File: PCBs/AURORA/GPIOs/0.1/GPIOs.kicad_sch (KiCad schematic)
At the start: 25 parts, among them J1 Conn_01x02_Pin, J10 Conn_01x02_Pin, J11 Conn_01x02_Pin, J12 Conn_01x02_Pin, J13 Conn_01x02_Pin, J14 Conn_01x02_Pin, J15 Conn_01x02_Pin, J16 Conn_01x02_Pin, J17 Conn_01x05_Pin, J2 Conn_01x02_Pin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

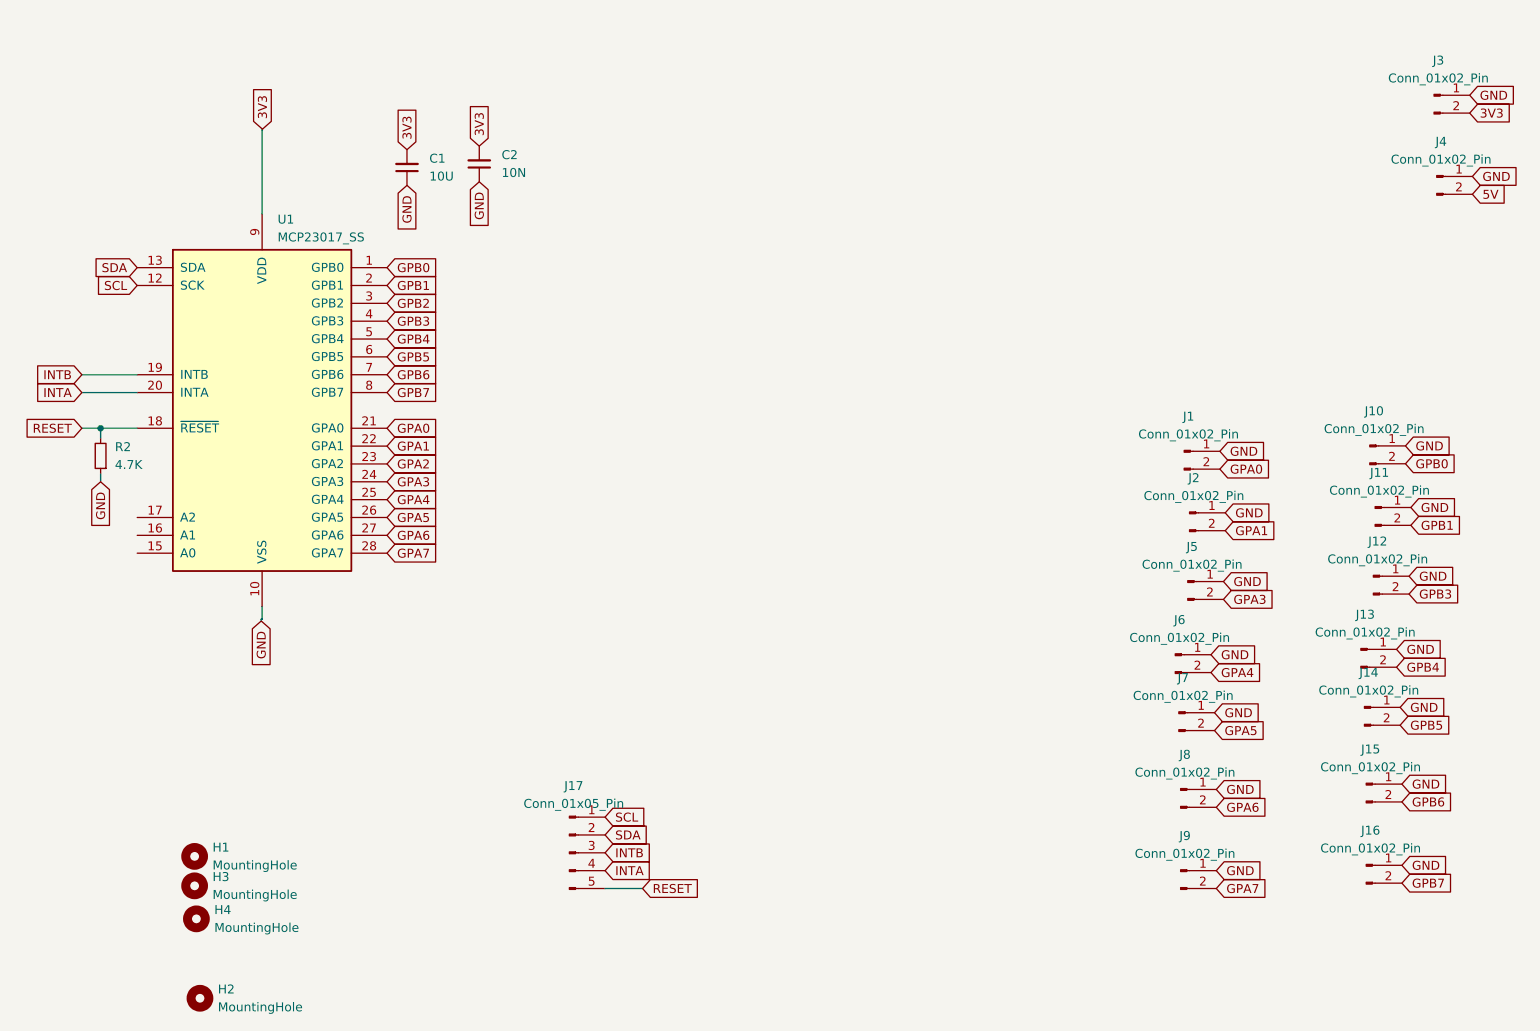
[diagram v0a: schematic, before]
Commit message: Fixing audio issues, leave TRUNC off and at 24 bits
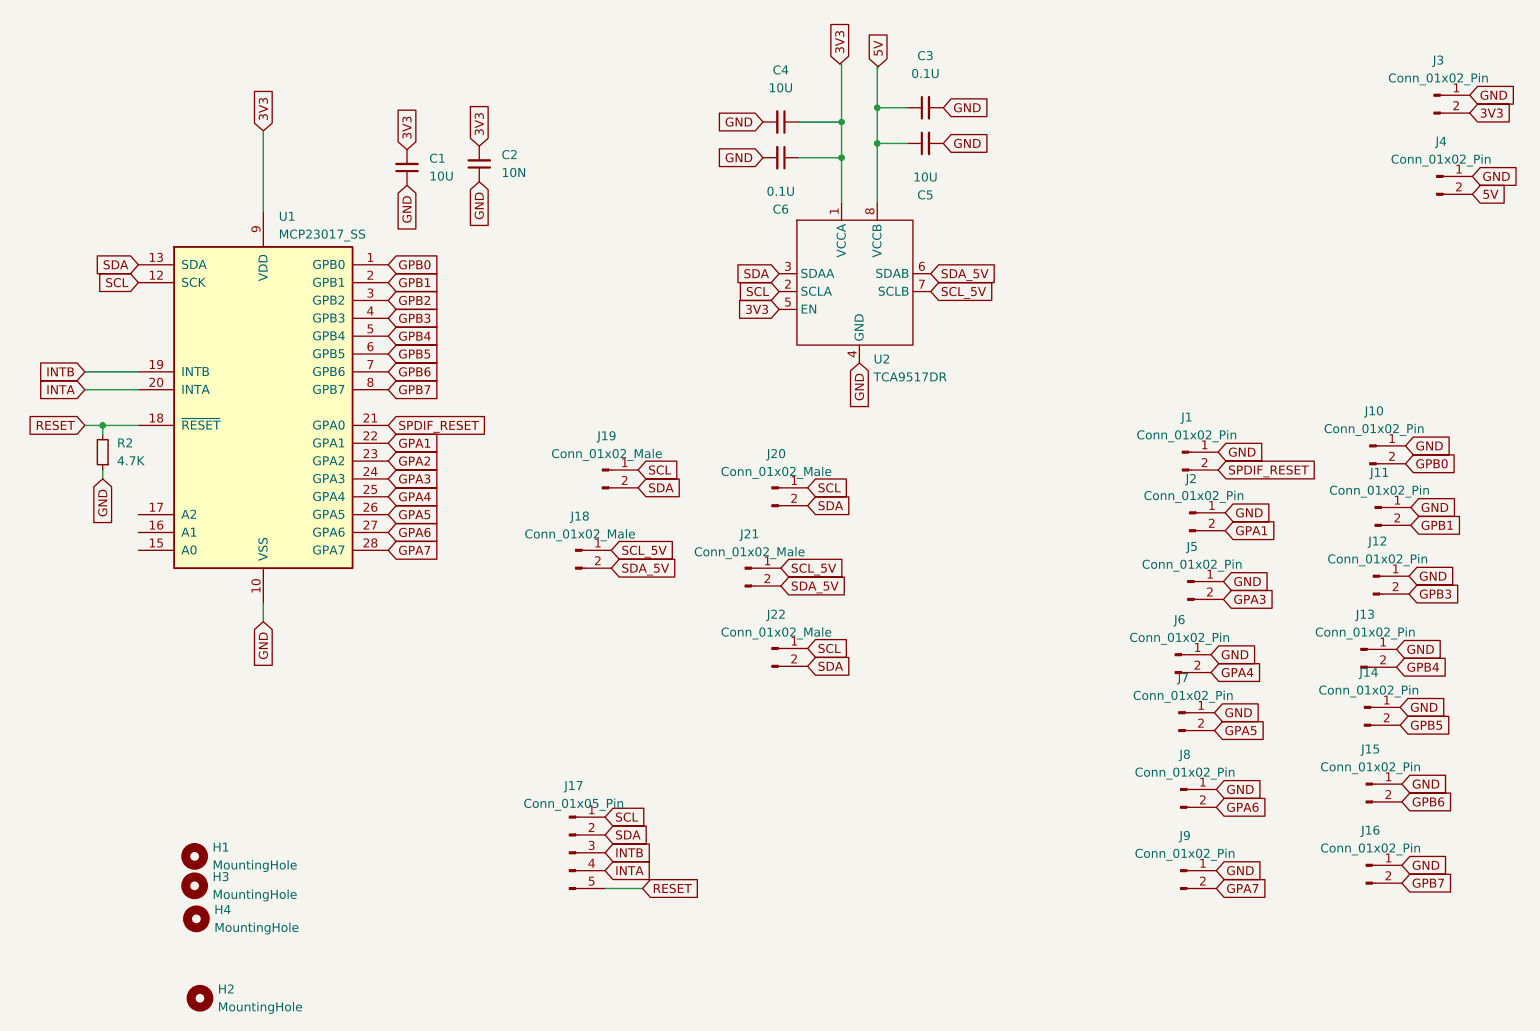
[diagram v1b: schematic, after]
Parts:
- added C3, C6: 0.1U, Capacitor_SMD:C_0805_2012Metric_Pad1.18x1.45mm_HandSolder, symbol Device:C_Small
- added C4, C5: 10U, Capacitor_SMD:C_1206_3216Metric_Pad1.33x1.80mm_HandSolder, symbol Device:C_Small
- added J18, J19, J20, J21, J22: Conn_01x02_Male, Connector_JST:JST_PH_B2B-PH-K_1x02_P2.00mm_Vertical, symbol Connector:Conn_01x02_Male
- added U2: TCA9517DR, Package_SO:SOIC-8_3.9x4.9mm_P1.27mm, symbol Interface_LineDriver:TCA9517DR
- J3: footprint Connector_JST:JST_PH_S2B-PH-SM4-TB_1x02-1MP_P2.00mm_Horizontal -> Connector_JST:JST_PH_B2B-PH-K_1x02_P2.00mm_Vertical
- J4: footprint Connector_JST:JST_PH_B2B-PH-SM4-TB_1x02-1MP_P2.00mm_Vertical -> Connector_JST:JST_PH_B2B-PH-K_1x02_P2.00mm_Vertical
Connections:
- net 3V3: now also C4.1, C6.1, U2.1 (VCCA), U2.5 (EN)
- net 5V: now also C3.1, C5.1, U2.8 (VCCB)
- net GND: now also C3.2, C4.2, C5.2, C6.2, U2.4 (GND)
- net SCL: now also J19.1 (Pin_1), J20.1 (Pin_1), J22.1 (Pin_1), U2.2 (SCLA)
- net SDA: now also J19.2 (Pin_2), J20.2 (Pin_2), J22.2 (Pin_2), U2.3 (SDAA)
- net GPA0 renamed SPDIF_RESET
- new net SCL_5V: J18.1 (Pin_1), J21.1 (Pin_1), U2.7 (SCLB)
- new net SDA_5V: J18.2 (Pin_2), J21.2 (Pin_2), U2.6 (SDAB)
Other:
- moved on the sheet: R2
